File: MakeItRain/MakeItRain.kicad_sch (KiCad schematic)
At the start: 15 parts, among them IC1 MCP23008T-E_SS, J1 Conn_02x14_Odd_Even, J2 Conn_02x19_Odd_Even, J3 Conn_01x19

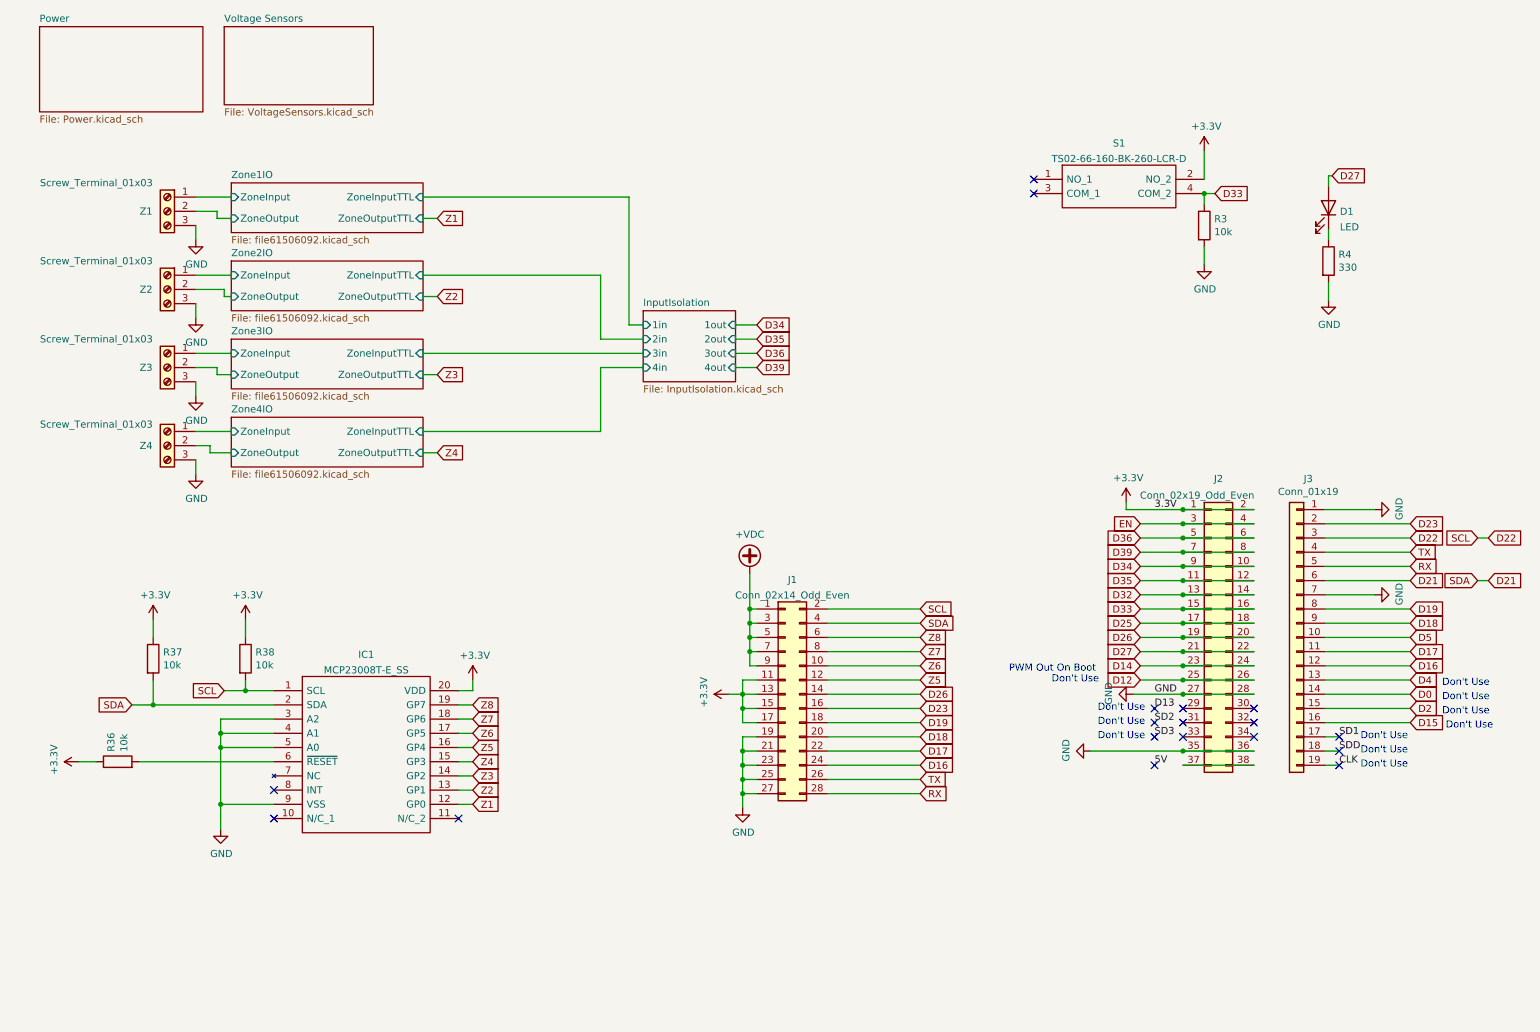
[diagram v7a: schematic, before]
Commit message: Moving into the prototyping testing this deisgn completely phase.
changes
* remapping some pins cause i forgot that ADC2 can not be used while using wifi.
* adding the TH version of the MCP230008 as i don't know the availability of these chips can populate one or the other
* removed zones 5-8 in the code since i hhaven't figured out the daughter board yet. Code not included can be buggy
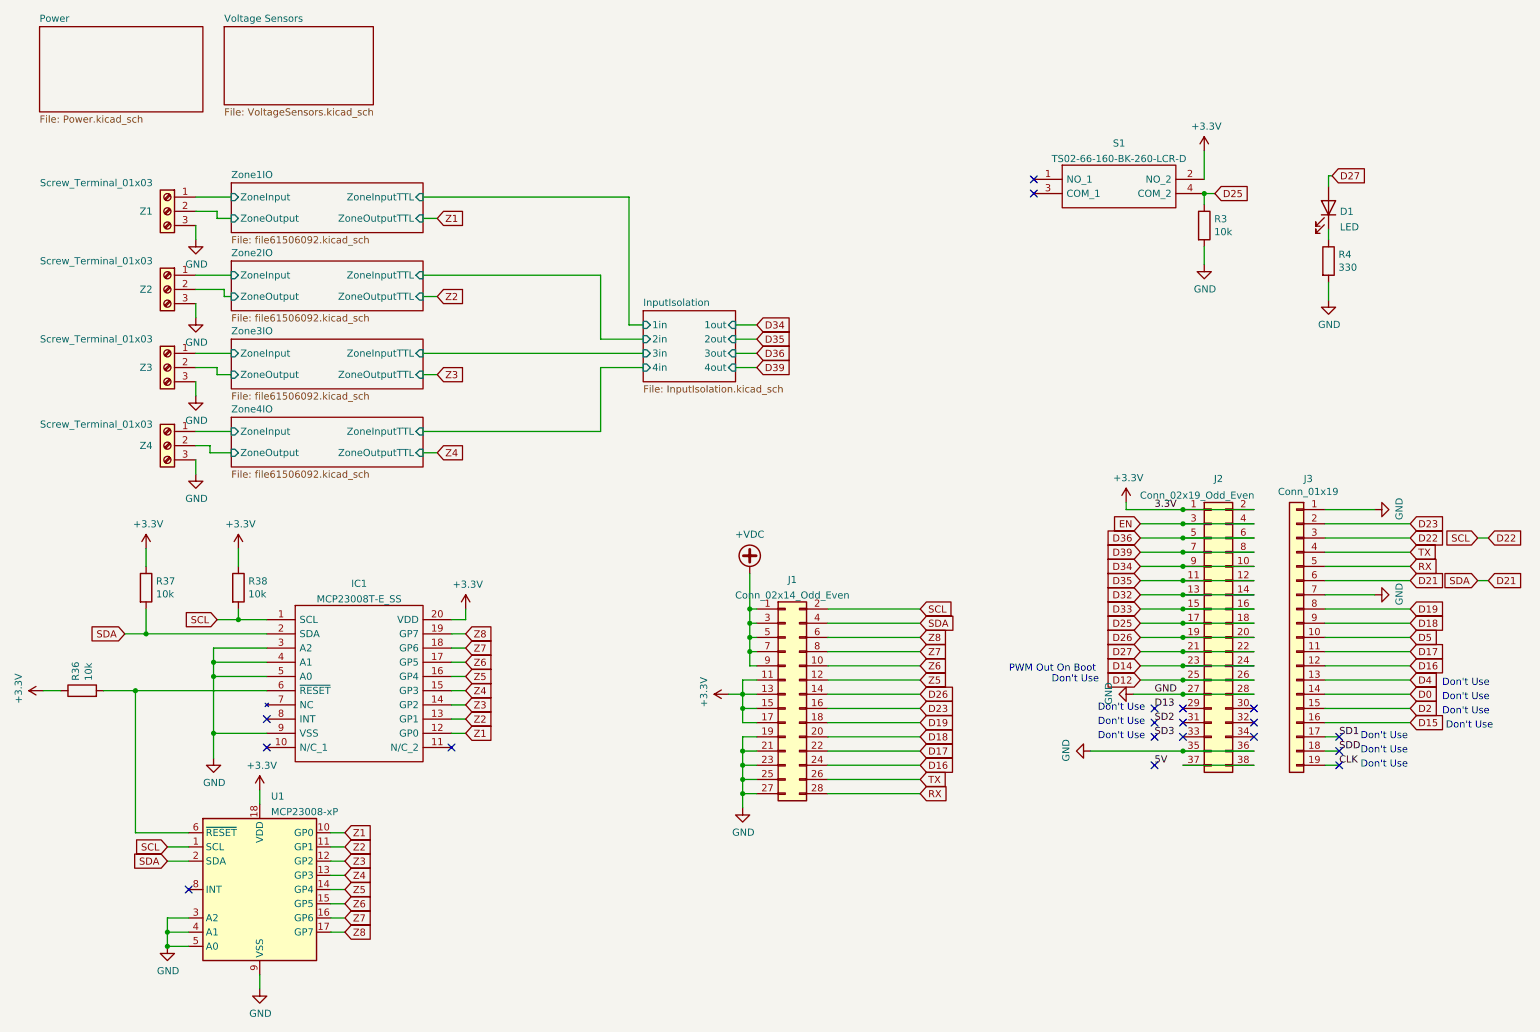
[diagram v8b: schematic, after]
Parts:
- added U1: MCP23008-xP, Package_DIP:DIP-18_W7.62mm, symbol Interface_Expansion:MCP23008-xP
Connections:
- net +3V3: now also U1.18 (VDD)
- net D21: now also U1.2 (SDA)
- net D22: now also U1.1 (SCL)
- net D25: now also R3.1, S1.4 (COM_2)
- net D33: no longer R3.1, S1.4 (COM_2)
- net GND: now also U1.3 (A2), U1.4 (A1), U1.5 (A0), U1.9 (VSS)
- net Z1: now also U1.10 (GP0)
- net Z2: now also U1.11 (GP1)
- net Z3: now also U1.12 (GP2)
- net Z4: now also U1.13 (GP3)
- net Z5: now also U1.14 (GP4)
- net Z6: now also U1.15 (GP5)
- net Z7: now also U1.16 (GP6)
- net Z8: now also U1.17 (GP7)
- net at IC1.6 (~{RESET}), R36.2: now also U1.6 (~{RESET})
- no-connect marks 18 -> 19
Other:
- moved on the sheet: IC1, R36, R37, R38
